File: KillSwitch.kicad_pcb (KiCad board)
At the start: 2 copper layers, 64 x 29.5 mm, 27 parts, among them J0 Screw_Terminal_1x04, J3 CONN_01X02, Q0 IRF1324PBF, Q1 IRF1324PBF, Q2 IRF1324PBF, Q3 IRF1324PBF, U0 NC7SZ08, U1 TPS62175, U2 4013

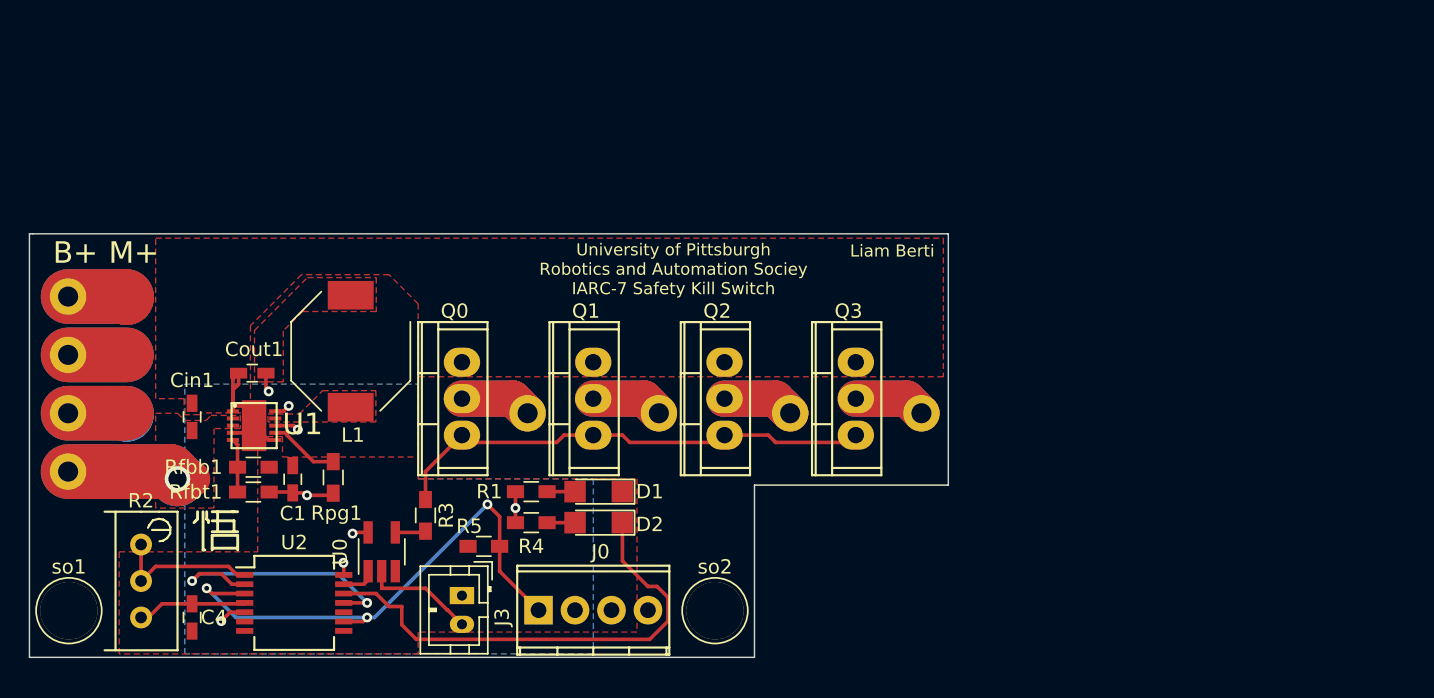
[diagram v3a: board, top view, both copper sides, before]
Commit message: Fixed Motor holes
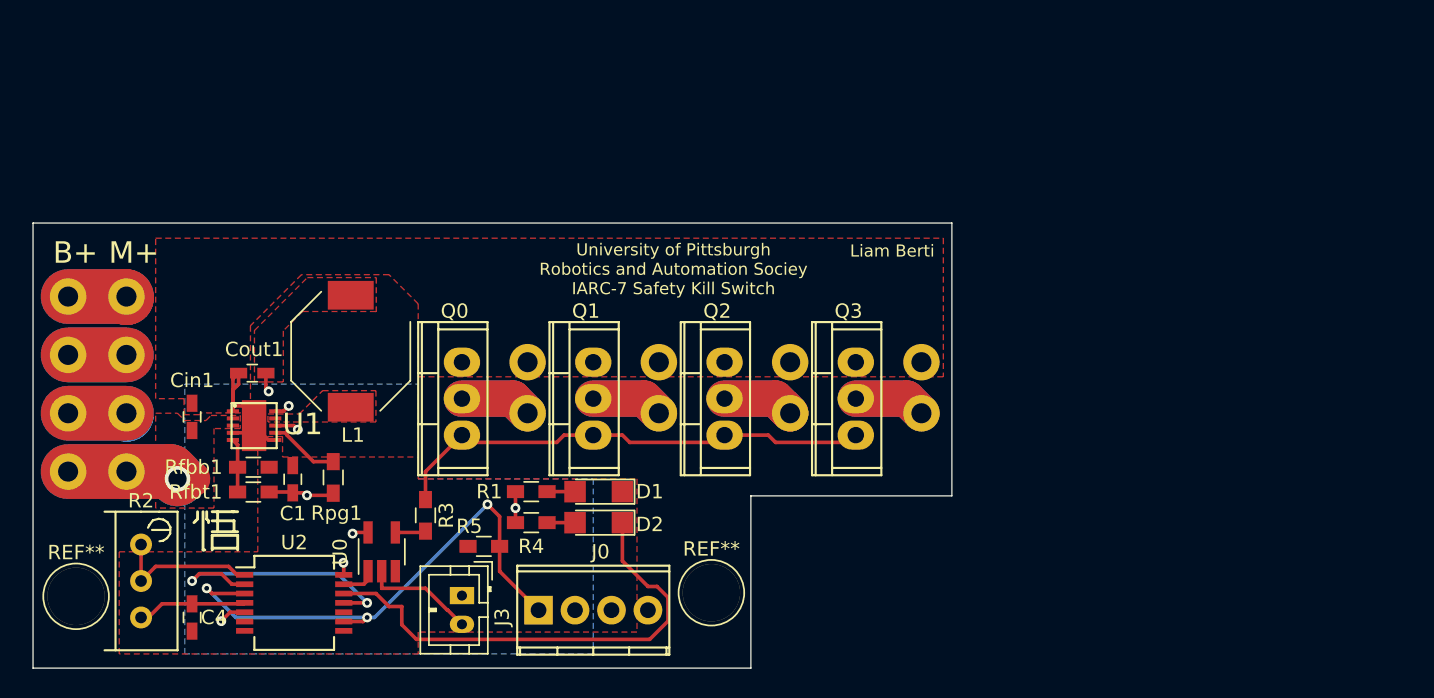
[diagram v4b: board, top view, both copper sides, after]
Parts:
- removed so1, so2: 1pin, UserParts:4mmhole
- added ?: CONN_01X08, Wire_Pads:barrel_connector, F.Cu at (157.9, 72.6)
- added REF**: 1pin, UserParts:4mmhole, F.Cu at (124.0, 92.0)
- added REF**: 1pin, UserParts:4mmhole, F.Cu at (168.2, 91.8)
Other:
- board size 64 x 29.5 mm -> 64 x 31 mm
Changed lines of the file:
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@@
 (kicad_pcb (version 4) (host pcbnew 4.0.6)
   (general
-    (links 61)
+    (links 69)
     (no_connects 0)
-    (area 120.699999 66.751999 184.835001 96.550001)
+    (area 120.949999 65.949999 185.050001 97.050001)
     (thickness 0.8128)
-    (drawings 32)
+    (drawings 29)
     (tracks 183)
     (zones 0)
-    (modules 27)
+    (modules 28)
     (nets 27)
   )
@@
   )
   (module Wire_Pads:barrel_connector (layer Top)
+    (at 157.861 72.644 180)
+    (fp_text reference "" (at -0.9525 11.176 180) (layer F.SilkS)
+      (effects (font (size 1 1) (thickness 0.15)))
+    )
+    (fp_text value CONN_01X08 (at 0 -0.5 180) (layer F.Fab)
+      (effects (font (size 1 1) (thickness 0.15)))
+    )
+    (pad 1 thru_hole circle (at -15.875 -3.048 180) (size 2.54 2.54) (drill 1.397) (layers *.Cu *.Mask)
+      (net 2 Earth))
+    (pad 2 thru_hole circle (at -25.019 -3.048 180) (size 2.54 2.54) (drill 1.397) (layers *.Cu *.Mask)
+      (net 2 Earth))
+    (pad 3 thru_hole circle (at -6.731 -3.048 180) (size 2.54 2.54) (drill 1.397) (layers *.Cu *.Mask)
+      (net 2 Earth))
+    (pad 4 thru_hole circle (at 2.413 -3.048 180) (size 2.54 2.54) (drill 1.397) (layers *.Cu *.Mask)
+      (net 2 Earth))
+    (pad 5 thru_hole circle (at 30.353 -10.668 180) (size 2.54 2.54) (drill 1.397) (layers *.Cu *.Mask)
+      (net 4 /VbattPos))
+    (pad 6 thru_hole circle (at 30.353 -6.604 180) (size 2.54 2.54) (drill 1.397) (layers *.Cu *.Mask)
+      (net 17 "Net-(J1-Pad6)"))
+    (pad 7 thru_hole circle (at 30.353 -2.54 180) (size 2.54 2.54) (drill 1.397) (layers *.Cu *.Mask)
+      (net 18 "Net-(J1-Pad7)"))
+    (pad 8 thru_hole circle (at 30.353 1.524 180) (size 2.54 2.54) (drill 1.397) (layers *.Cu *.Mask)
+      (net 19 "Net-(J1-Pad8)"))
+  )
+  (module Wire_Pads:barrel_connector (layer Top)
     (at 169.164 57.912)
     (fp_text reference "" (at 0 0.5) (layer F.SilkS)
@@
     (pad 8 thru_hole circle (at 13.716 21.336) (size 2.54 2.54) (drill 1.397) (layers *.Cu *.Mask)
       (net 23 "Net-(J2-Pad8)"))
+  )
+  (module UserParts:4mmhole (layer Top)
+    (at 124 92)
+    (descr "module 1 pin (ou trou mecanique de percage)")
+    (tags DEV)
+    (fp_text reference REF** (at 0 -3.048) (layer F.SilkS)
+      (effects (font (size 1 1) (thickness 0.15)))
+    )
+    (fp_text value 1pin (at 0 3) (layer F.Fab)
+      (effects (font (size 1 1) (thickness 0.15)))
+    )
+    (fp_circle (center 0 0) (end 2 0.8) (layer F.Fab) (width 0.1))
+    (fp_circle (center 0 0) (end 2.6 0) (layer F.CrtYd) (width 0.05))
+    (fp_circle (center 0 0) (end 0 -2.286) (layer F.SilkS) (width 0.12))
+    (pad 1 thru_hole circle (at 0 0) (size 4 4) (drill 4) (layers *.Cu *.Mask))
   )
   (module Capacitors_SMD:C_0603_HandSoldering (layer Top)
@@
   )
   (module UserParts:4mmhole (layer Top)
-    (at 123.5 93)
+    (at 168.25 91.75)
     (descr "module 1 pin (ou trou mecanique de percage)")
     (tags DEV)
-    (fp_text reference so1 (at 0 -3.048) (layer F.SilkS)
+    (fp_text reference REF** (at 0 -3.048) (layer F.SilkS)
       (effects (font (size 1 1) (thickness 0.15)))
     )
@@
     (pad 1 thru_hole circle (at 0 0) (size 4 4) (drill 4) (layers *.Cu *.Mask))
   )
-  (module UserParts:4mmhole (layer Top)
-    (at 168.5 93)
-    (descr "module 1 pin (ou trou mecanique de percage)")
-    (tags DEV)
-    (fp_text reference so2 (at 0 -3.048) (layer F.SilkS)
-      (effects (font (size 1 1) (thickness 0.15)))
-    )
-    (fp_text value 1pin (at 0 3) (layer F.Fab)
-      (effects (font (size 1 1) (thickness 0.15)))
-    )
-    (fp_circle (center 0 0) (end 2 0.8) (layer F.Fab) (width 0.1))
-    (fp_circle (center 0 0) (end 2.6 0) (layer F.CrtYd) (width 0.05))
-    (fp_circle (center 0 0) (end 0 -2.286) (layer F.SilkS) (width 0.12))
-    (pad 1 thru_hole circle (at 0 0) (size 4 4) (drill 4) (layers *.Cu *.Mask))
-  )
-  (gr_line (start 120.75 66.75) (end 120.75 96.25) (angle 90) (layer Edge.Cuts) (width 0.1))
-  (gr_line (start 121 66.75) (end 120.75 66.75) (angle 90) (layer Edge.Cuts) (width 0.1))
-  (gr_line (start 184.75 66.75) (end 121 66.75) (angle 90) (layer Edge.Cuts) (width 0.1))
-  (gr_line (start 184.75 84.25) (end 184.75 66.75) (angle 90) (layer Edge.Cuts) (width 0.1))
-  (gr_line (start 171.25 84.25) (end 184.75 84.25) (angle 90) (layer Edge.Cuts) (width 0.1))
-  (gr_line (start 171.25 96.25) (end 171.25 84.25) (angle 90) (layer Edge.Cuts) (width 0.1))
-  (gr_line (start 120.75 96.25) (end 171.25 96.25) (angle 90) (layer Edge.Cuts) (width 0.1))
-  (dimension 45 (width 0.3) (layer Eco1.User)
-    (gr_text "45.000 mm" (at 146 100.85) (layer Eco1.User)
+  (gr_line (start 185 85) (end 185 66) (angle 90) (layer Edge.Cuts) (width 0.1))
+  (gr_line (start 171 85) (end 185 85) (angle 90) (layer Edge.Cuts) (width 0.1))
+  (gr_line (start 171 97) (end 171 85) (angle 90) (layer Edge.Cuts) (width 0.1))
+  (gr_line (start 121 97) (end 171 97) (angle 90) (layer Edge.Cuts) (width 0.1))
+  (gr_line (start 121 66) (end 121 97) (angle 90) (layer Edge.Cuts) (width 0.1))
+  (gr_line (start 185 66) (end 121 66) (angle 90) (layer Edge.Cuts) (width 0.1))
+  (dimension 50.8 (width 0.3) (layer Eco2.User)
+    (gr_text "2.0000 in" (at 185.42 154.94) (layer Eco2.User)
       (effects (font (size 1.5 1.5) (thickness 0.3)))
     )
-    (feature1 (pts (xy 123.5 93) (xy 123.5 102.2)))
-    (feature2 (pts (xy 168.5 93) (xy 168.5 102.2)))
-    (crossbar (pts (xy 168.5 99.5) (xy 123.5 99.5)))
-    (arrow1a (pts (xy 123.5 99.5) (xy 124.626504 98.913579)))
-    (arrow1b (pts (xy 123.5 99.5) (xy 124.626504 100.086421)))
-    (arrow2a (pts (xy 168.5 99.5) (xy 167.373496 98.913579)))
-    (arrow2b (pts (xy 168.5 99.5) (xy 167.373496 100.086421)))
-  )
-  (dimension 4 (width 0.3) (layer Eco1.User)
-    (gr_text "4.000 mm" (at 175.35 93 90) (layer Eco1.User)
-      (effects (font (size 1.5 1.5) (thickness 0.3)))
-    )
-    (feature1 (pts (xy 169 91) (xy 176.7 91)))
-    (feature2 (pts (xy 169 95) (xy 176.7 95)))
-    (crossbar (pts (xy 174 95) (xy 174 91)))
-    (arrow1a (pts (xy 174 91) (xy 174.586421 92.126504)))
-    (arrow1b (pts (xy 174 91) (xy 173.413579 92.126504)))
-    (arrow2a (pts (xy 174 95) (xy 174.586421 93.873496)))
-    (arrow2b (pts (xy 174 95) (xy 173.413579 93.873496)))
-  )
-  (dimension 4 (width 0.3) (layer Eco1.User)
-    (gr_text "4.000 mm" (at 115.65 93 90) (layer Eco1.User)
-      (effects (font (size 1.5 1.5) (thickness 0.3)))
-    )
-    (feature1 (pts (xy 123 91) (xy 114.3 91)))
-    (feature2 (pts (xy 123 95) (xy 114.3 95)))
-    (crossbar (pts (xy 117 95) (xy 117 91)))
-    (arrow1a (pts (xy 117 91) (xy 117.586421 92.126504)))
-    (arrow1b (pts (xy 117 91) (xy 116.413579 92.126504)))
-    (arrow2a (pts (xy 117 95) (xy 117.586421 93.873496)))
-    (arrow2b (pts (xy 117 95) (xy 116.413579 93.873496)))
+    (feature1 (pts (xy 160.02 154.94) (xy 160.02 154.94)))
+    (feature2 (pts (xy 210.82 154.94) (xy 210.82 154.94)))
+    (crossbar (pts (xy 210.82 154.94) (xy 160.02 154.94)))
+    (arrow1a (pts (xy 160.02 154.94) (xy 161.146504 154.353579)))
+    (arrow1b (pts (xy 160.02 154.94) (xy 161.146504 155.526421)))
+    (arrow2a (pts (xy 210.82 154.94) (xy 209.693496 154.353579)))
+    (arrow2b (pts (xy 210.82 154.94) (xy 209.693496 155.526421)))
   )
   (gr_line (start 133.477 88.646) (end 135.255 88.646) (angle 90) (layer F.SilkS) (width 0.2))

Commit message: new switch
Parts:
- removed ? (x2): CONN_01X08, Wire_Pads:barrel_connector
- removed Cin1: 2.2uF, Capacitors_SMD:C_0603_HandSoldering
- removed L1: 10uH, 0.036Ohm, Inductors:Inductor_Bourns-SRU8043
- removed REF** (x2): 1pin, UserParts:4mmhole
- removed Rfbb1: 383k, Resistors_SMD:R_0603_HandSoldering
- removed Rfbt1: 2Meg, Resistors_SMD:R_0603_HandSoldering
- removed Rpg1: 100k, Resistors_SMD:R_0603_HandSoldering
- removed U1: TPS62175, Housings_SON:SON-10
- added J1: CONN_01X04, Wire_Pads:barrel_connector, F.Cu at (189.0, 56.0)
- added J2: CONN_01X04, Wire_Pads:barrel_connector, F.Cu at (218.0, 51.0)
- added J4: CONN_01X04, Socket_Strips:Socket_Strip_Straight_1x04_Pitch1.27mm, F.Cu at (184.0, 94.0)
- U2: footprint Housings_SSOP:SSOP-14_5.3x6.2mm_Pitch0.65mm -> Housings_DIP:DIP-14_W7.62mm_LongPads
- moved R3 61.6 mm to (208.0, 71.0)
- moved Cout1 60.5 mm to (196.0, 86.0), turned to 270 degrees
- moved U0 56.8 mm to (202.0, 85.0)
- moved R2 53.7 mm to (180.0, 73.0)
- moved U2 50.9 mm to (185.7, 71.8)
- moved R1 49.7 mm to (204.0, 73.0), turned to 0 degrees
- moved C4 49.5 mm to (181.0, 86.0), turned to 0 degrees
- moved R4 49.3 mm to (204.0, 77.0), turned to 180 degrees
- moved J3 49.1 mm to (200.0, 93.0), turned to 0 degrees
- moved R5 46.2 mm to (198.0, 81.0), turned to 0 degrees
- moved C1 42.5 mm to (181.0, 91.0), turned to 0 degrees
- moved D1 40.3 mm to (199.0, 73.0), turned to 0 degrees
- moved D2 39.8 mm to (199.0, 77.0), turned to 0 degrees
- moved Q3 36.1 mm to (211.0, 63.0)
- moved Q2 35.3 mm to (201.0, 63.0)
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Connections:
- J0 pad 4: Net-(J0-Pad4) -> (no net)
- U2 pad 7: VSS -> Earth
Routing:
- net /AND1: track 2.41 -> 33.1 mm
- net Net-(D2-Pad1): track 33.7 -> 4.36 mm
- net /VbattPos: track 18.1 -> 0.00 mm, vias 2 -> 0
- net Earth: track 13.6 -> 0.00 mm
- net Net-(J1-Pad8): track 12.4 -> 0.00 mm
- net Net-(J1-Pad6): track 12.3 -> 0.00 mm
- net /GATE: track 34.2 -> 46.0 mm
- net Net-(R3-Pad2): track 2.14 -> 13.9 mm
- net /PWM: track 37.0 -> 26.6 mm, vias 3 -> 0
- net Net-(U2-Pad11): track 19.0 -> 9.72 mm, vias 2 -> 0
- net Net-(J1-Pad7): track 8.13 -> 0.00 mm
- net Net-(J2-Pad4): track 11.4 -> 4.83 mm
- net Net-(J2-Pad2): track 11.4 -> 4.83 mm
- net Net-(C4-Pad1): track 7.73 -> 14.2 mm
- net Net-(J2-Pad1): track 9.99 -> 4.83 mm
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- removed copper zone on F.Cu, net +5V
- removed copper zone on F.Cu, net /VbattPos
- removed copper zone on F.Cu, net Net-(L1-Pad2)
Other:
- board size 64 x 31 mm -> 40.5 x 40 mm
- board text removed: "B+"
- board text removed: "Liam Berti"
- board text removed: "M+"
- board text removed: "University of Pittsburgh Robotics and Automation Sociey IARC-7 Safety Kill Switch"

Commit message: Added features
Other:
- board text added: "Liam Berti IARC7 Safety Switch Pitt RAS"
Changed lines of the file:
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@@
     (area 175.949999 56.949999 216.550001 97.050001)
     (thickness 0.8128)
-    (drawings 9)
+    (drawings 10)
     (tracks 74)
     (zones 0)
@@
       (net 17 "Net-(J2-Pad4)"))
   )
+  (gr_text "Liam Berti\nIARC7 Safety Switch\nPitt RAS" (at 206.2 88.8 90) (layer F.SilkS)
+    (effects (font (size 0.8 0.8) (thickness 0.125)))
+  )
   (gr_line (start 205 97) (end 205.5 97) (angle 90) (layer Edge.Cuts) (width 0.1))

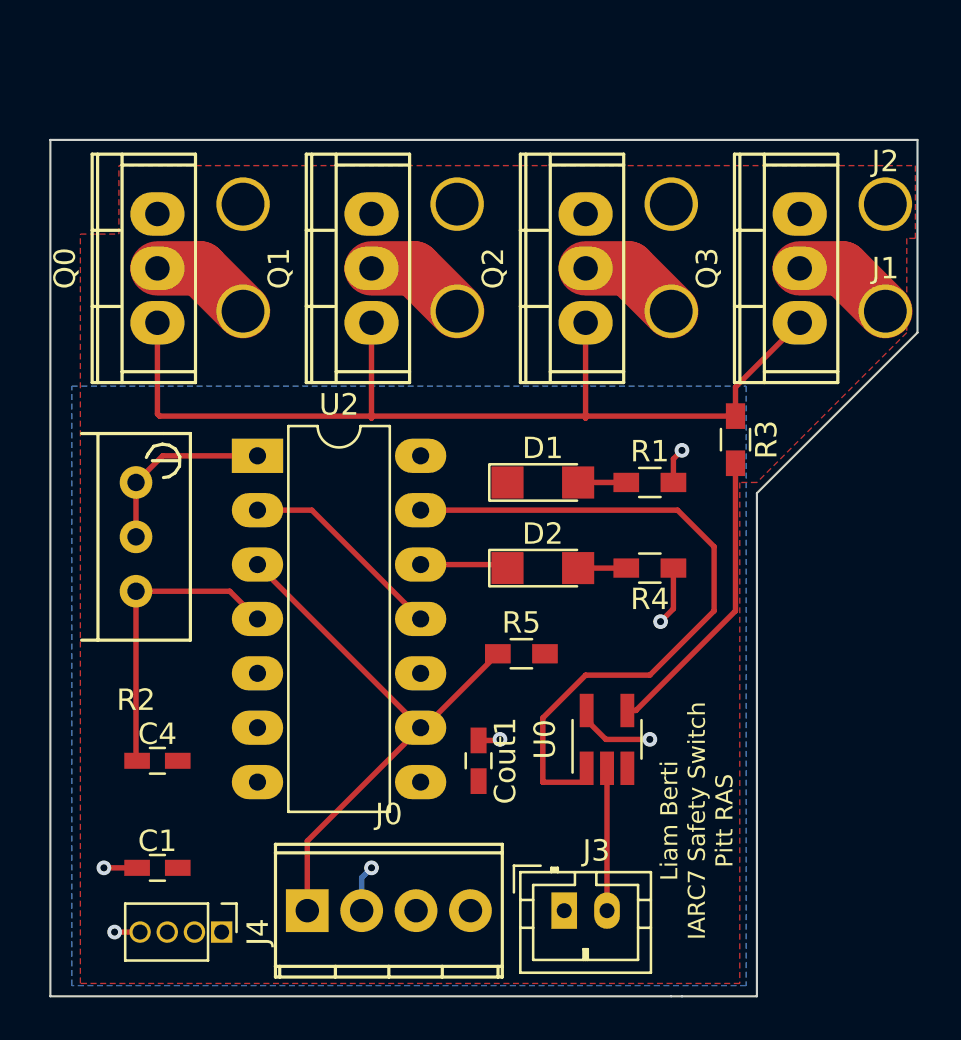
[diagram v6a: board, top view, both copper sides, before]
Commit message: Add varistors to DS
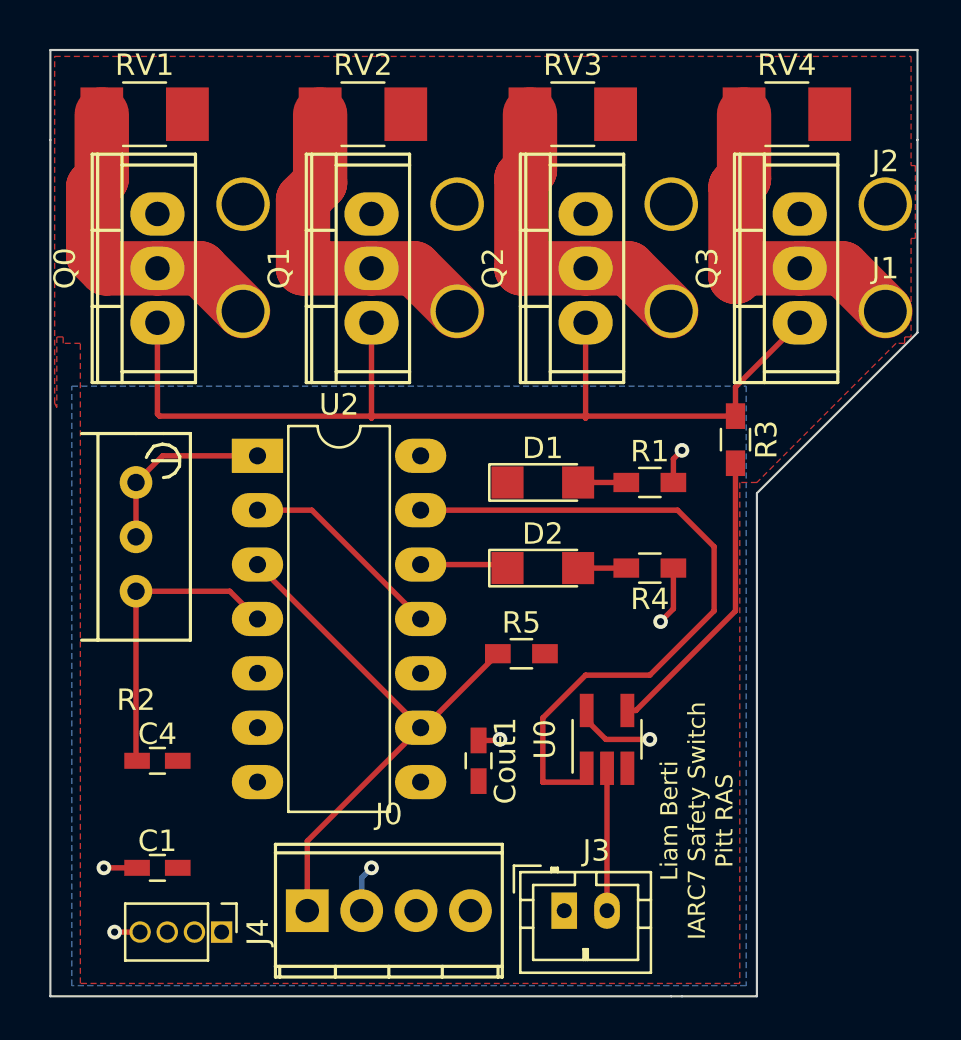
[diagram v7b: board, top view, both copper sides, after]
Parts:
- added RV1: Varistor, Resistors_SMD:R_1210_HandSoldering, F.Cu at (180.4, 55.8)
- added RV2: Varistor, Resistors_SMD:R_1210_HandSoldering, F.Cu at (190.6, 55.8)
- added RV3: Varistor, Resistors_SMD:R_1210_HandSoldering, F.Cu at (200.4, 55.8)
- added RV4: Varistor, Resistors_SMD:R_1210_HandSoldering, F.Cu at (210.4, 55.8)
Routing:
- net Net-(J2-Pad1): track 4.83 -> 15.8 mm
- net Net-(J2-Pad3): track 4.83 -> 15.6 mm
- net Net-(J2-Pad2): track 4.83 -> 15.2 mm
- net Net-(J2-Pad4): track 4.83 -> 14.8 mm
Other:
- board size 40.5 x 40 mm -> 40.5 x 44.2 mm
